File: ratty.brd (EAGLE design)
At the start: 616 x 652 mm, 90 parts, among them IC2 L293DD, Q1 BS170, Q2 BS170, Q3 BS170, Q5 BS170, U1 ITG-32001:1

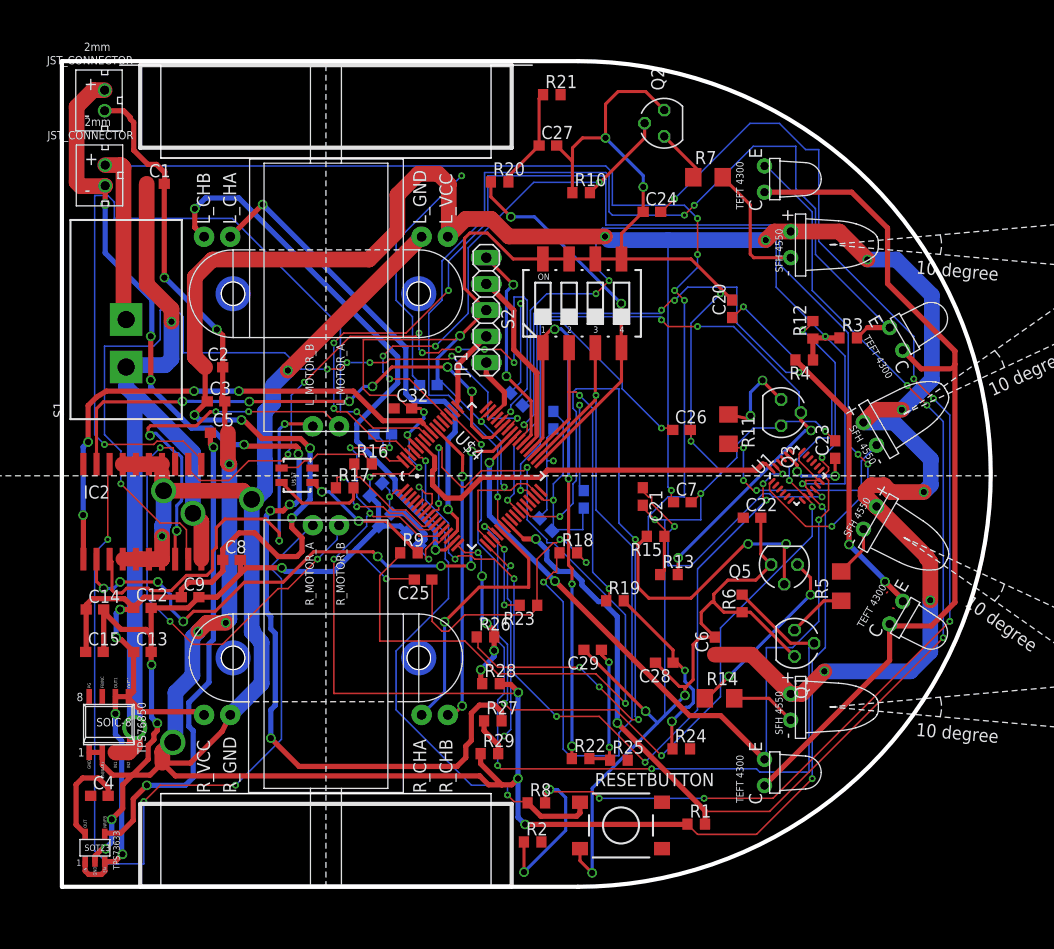
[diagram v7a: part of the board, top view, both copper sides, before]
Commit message: Changed schematic a bit to make it easier to route
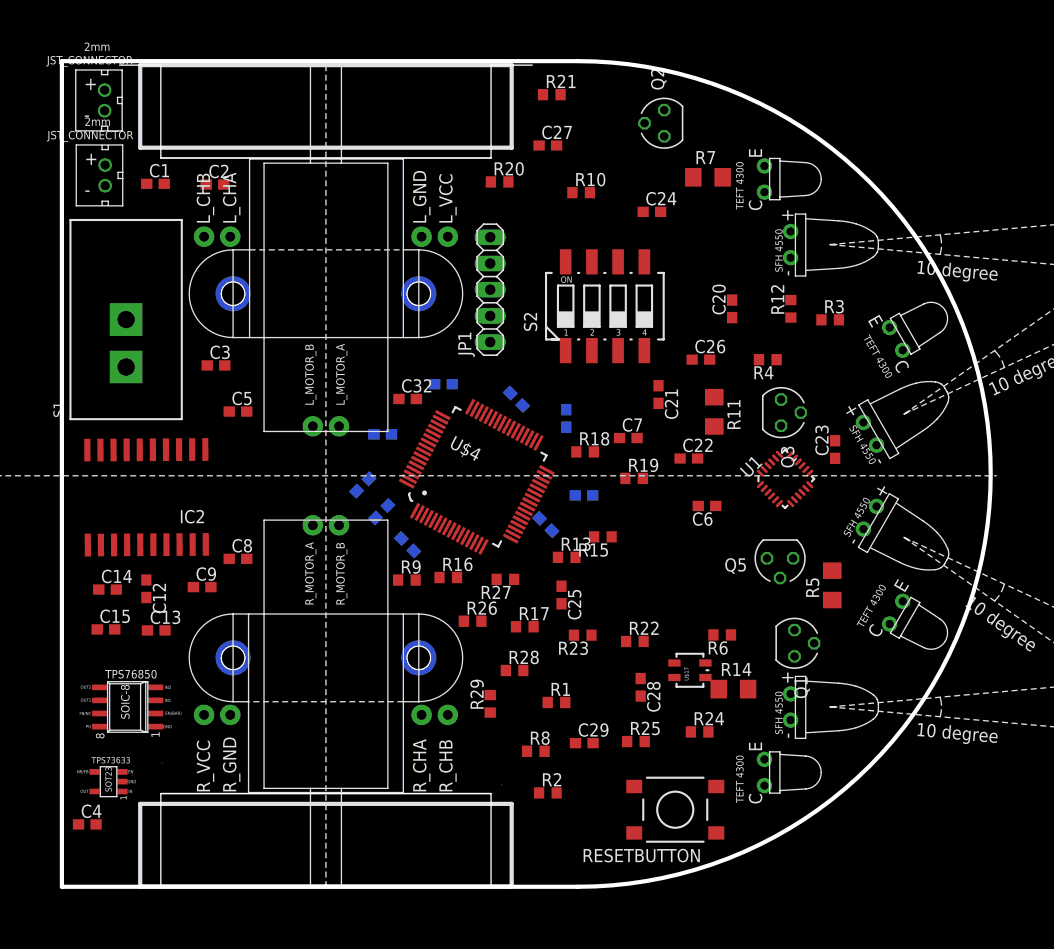
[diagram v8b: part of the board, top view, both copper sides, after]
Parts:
- moved U$17 42.5 mm to (60.9, 21.0)
- moved R17 22.0 mm to (44.9, 25.2)
- moved R1 17.9 mm to (47.9, 17.9)
- moved C2 17.7 mm to (14.8, 68.0)
- moved R27 13.8 mm to (43.0, 29.8), turned to 180 degrees
- moved R16 13.8 mm to (37.4, 30.0)
- moved C6 13.6 mm to (62.5, 36.9), turned to 180 degrees
- moved C25 13.5 mm to (48.4, 28.3), turned to 270 degrees
- moved R22 12.5 mm to (55.5, 23.8)
- moved R19 12.0 mm to (55.4, 39.6)
- moved R13 10.0 mm to (48.9, 31.9)
- moved C21 10.00 mm to (57.8, 47.7)
- moved R18 9.91 mm to (50.7, 42.1)
- moved C29 9.08 mm to (50.6, 13.9), turned to 0 degrees
- moved C22 8.39 mm to (60.8, 41.5)
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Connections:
- removed net PA_0_ENCODER1_1: U$4.14, U$8.L_CHA
- removed net PA_1_ENCODER1_2: U$4.15, U$8.L_CHB
- removed net PA_5_ENCODER2_1: U$4.21, U$8.R_CHA
- removed net PB3_ENCODER2_2: U$4.55, U$8.R_CHB
- removed net PB7_I2CSDA_FOR_GYRO: U$4.59, U1.24
- removed net PB8_I2C1SCL_FOR_GYRO: U$4.61, U1.23
- removed net PB9_GYROCLK: U$4.62, U1.1
- new net ENCODER1_1: U$4.21, U$8.L_CHA
- new net ENCODER1_2: U$4.55, U$8.L_CHB
- new net ENCODER2_1: U$4.14, U$8.R_CHA
- new net ENCODER2_2: U$4.15, U$8.R_CHB
- new net GYROCLK: U$4.42, U1.1
- new net I2CSCL_FOR_GYRO: U$4.41, U1.23
- new net I2CSDA_FOR_GYRO: U$4.40, U1.24
- net L_DIGITAL_IN_1: now also U$4.59; no longer U$4.41
- net L_DIGITAL_IN_2: now also U$4.61; no longer U$4.42
- net PC9_REC_CIRCUIT_4: now also U$4.53; no longer U$4.40
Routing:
- net DGND: track 380.1 -> 0.00 mm, vias 22 -> 0
- net 5V: track 301.8 -> 0.00 mm, vias 16 -> 0
- net AGND: track 223.0 -> 0.00 mm, vias 13 -> 0
- net BATTERY_1: track 150.6 -> 0.00 mm, vias 7 -> 0
- net N$2: track 132.4 -> 0.00 mm, vias 8 -> 0
- net GND: track 127.1 -> 0.00 mm, vias 8 -> 0
- net PA_7_REC_CIRCUIT_1: track 121.9 -> 0.00 mm, vias 5 -> 0
- net PB9_GYROCLK: track 117.0 -> 0.00 mm, vias 6 -> 0
- net BATTERY_2: track 112.1 -> 0.00 mm, vias 8 -> 0
- net PA_6_REC_CIRCUIT_2: track 102.3 -> 0.00 mm, vias 3 -> 0
- net GYROVLOGIC: track 95.4 -> 0.00 mm, vias 6 -> 0
- net PC9_REC_CIRCUIT_4: track 94.7 -> 0.00 mm, vias 5 -> 0
- net MGND: track 89.9 -> 0.00 mm, vias 4 -> 0
- net PC_10_EMIT_CIRCUIT_1: track 88.8 -> 0.00 mm, vias 3 -> 0
- net RIGHT_FORWARD: track 88.0 -> 0.00 mm, vias 3 -> 0
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- removed copper zone on layer 1, net 3.3V
- removed copper zone on layer 16, net GND
